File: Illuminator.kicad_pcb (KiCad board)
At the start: 2 copper layers, 60 x 60 mm, 22 parts, among them J0 Conn_01x03_Male, Q0 DMG1012UW

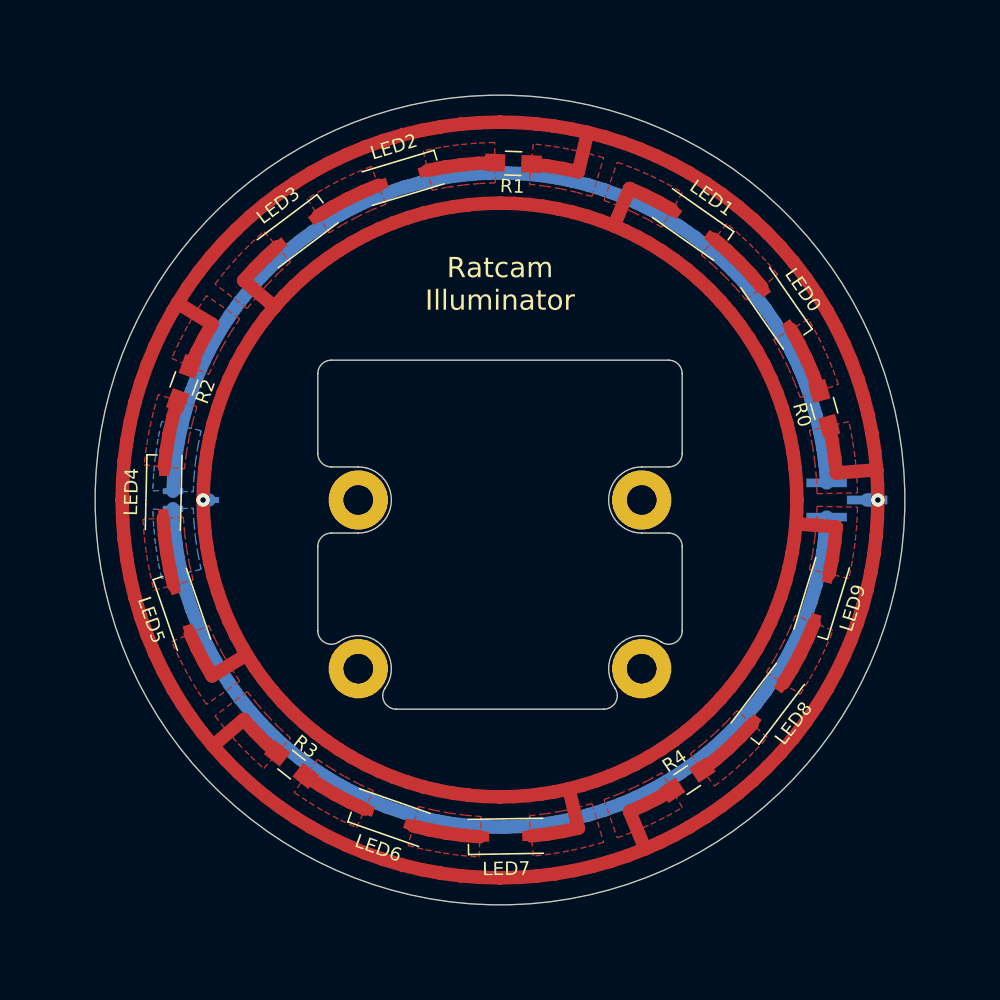
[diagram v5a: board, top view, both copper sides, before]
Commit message: Routing and placing everything from scratch.
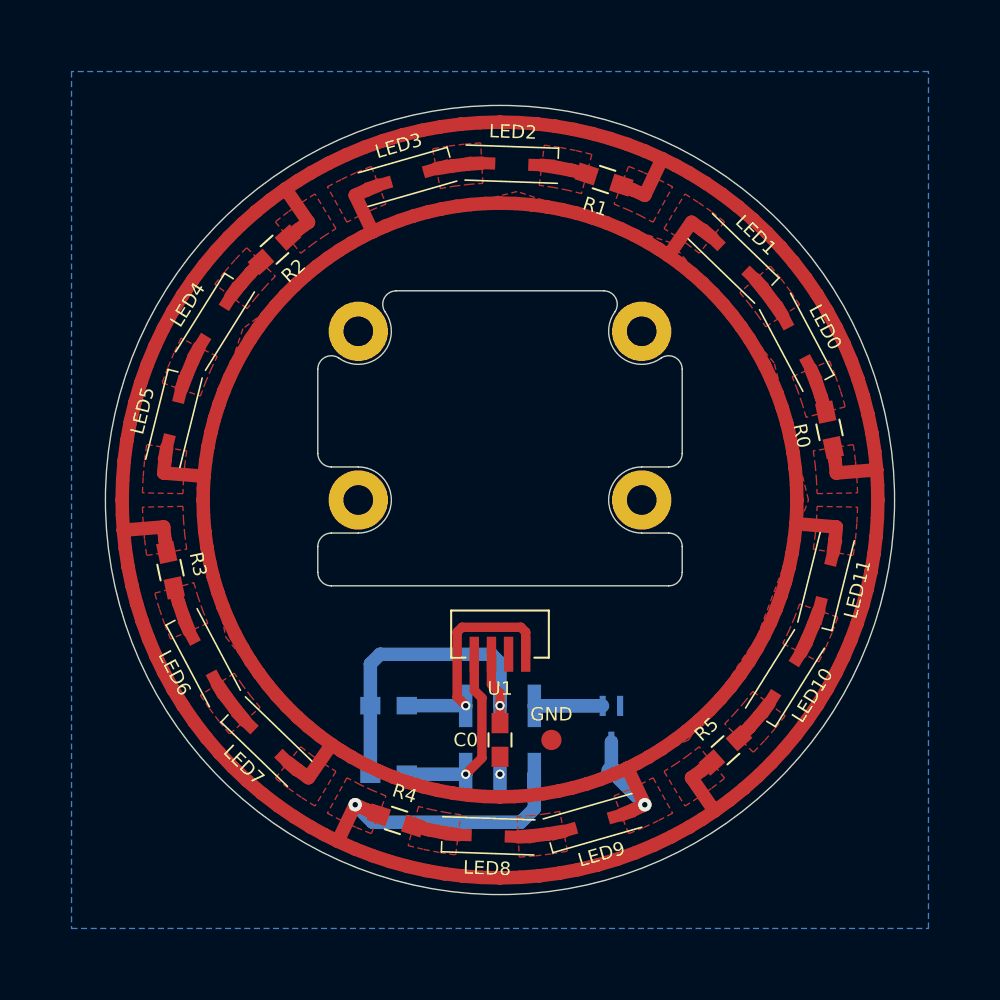
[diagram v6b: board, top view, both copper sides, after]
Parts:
- removed QRCode: http://bit.ly/2m9yLHR, Ratcam:QRCode
- removed the REF** at (110.5, 112.5)
- removed the REF** at (89.5, 112.5)
- added C0: 100nF, Capacitors_SMD:C_0805_HandSoldering, F.Cu at (100.0, 117.8)
- added GND: Measurement_Point_Round-SMD-Pad_Small, Measurement_Points:Measurement_Point_Round-SMD-Pad_Small, F.Cu at (103.8, 117.8)
- added LED: Measurement_Point_Round-SMD-Pad_Small, Measurement_Points:Measurement_Point_Round-SMD-Pad_Small, B.Cu at (108.3, 120.1)
- added LED10: VSMY2850G, Ratcam:LED-GW_2.3x2.3mm_HandSoldering, F.Cu at (121.1, 113.2)
- added LED11: VSMY2850G, Ratcam:LED-GW_2.3x2.3mm_HandSoldering, F.Cu at (124.2, 106.0)
- added R5: 15, Resistors_SMD:R_0805_HandSoldering, F.Cu at (116.7, 118.5)
- added REF**: MountingHole_2.2mm_M2, Mounting_Holes:MountingHole_2.2mm_M2_Pad, F.Cu at (110.5, 87.5)
- added REF**: MountingHole_2.2mm_M2, Mounting_Holes:MountingHole_2.2mm_M2_Pad, F.Cu at (89.5, 87.5)
- added R_PU1: 4.7KΩ, Resistors_SMD:R_0805_HandSoldering, B.Cu at (91.7, 120.3)
- added R_PU2: 4.7KΩ, Resistors_SMD:R_0805_HandSoldering, B.Cu at (91.7, 115.2)
- added U1: VEML7700, Ratcam:VEML7700, F.Cu at (100.0, 111.4)
- J0: value Conn_01x03_Male -> Conn_02x03_Top_Bottom; footprint Pin_Headers:Pin_Header_Straight_1x03_Pitch1.27mm_SMD_Pin1Left -> Pin_Headers:Pin_Header_Straight_2x03_Pitch2.54mm_SMD
- LED0, LED1, LED2, LED3, LED4, LED5, LED6, LED7, LED8, LED9: footprint Ratcam:LED-GW_2.3x2.3mm -> Ratcam:LED-GW_2.3x2.3mm_HandSoldering
- REF** (x2): value MountingHole_2.2mm_M2_Pad -> MountingHole_2.2mm_M2
- moved Q0 35.3 mm to (108.3, 116.6), turned to 270 degrees
- moved J0 31.3 mm to (100.0, 117.8), turned to 90 degrees
- moved LED9 23.8 mm to (106.9, 123.9), turned to 195.975 degrees
- moved LED8 22.9 mm to (99.1, 124.9), turned to 177.989 degrees
- moved R4 21.8 mm to (92.3, 123.7), turned to 342.015 degrees
- moved LED7 19.1 mm to (82.7, 117.9), turned to 135.975 degrees
- moved LED6 18.2 mm to (78.0, 111.7), turned to 117.989 degrees
- moved R3 17.0 mm to (75.6, 105.2), turned to 282.015 degrees
- moved LED5 14.2 mm to (75.8, 94.0), turned to 75.9747 degrees
- moved LED4 13.2 mm to (78.9, 86.8), turned to 57.9894 degrees
- moved R2 12.0 mm to (83.3, 81.5), turned to 222.015 degrees
- moved LED3 9.08 mm to (93.1, 76.1), turned to 15.9747 degrees
- moved LED2 8.12 mm to (100.9, 75.1), turned to 357.989 degrees
- moved R1 6.84 mm to (107.7, 76.3), turned to 162.015 degrees
- moved LED1 3.91 mm to (117.3, 82.1), turned to 315.975 degrees
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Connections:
- J0 pad 1: /TO_3V3 -> /TO_5V
- J0 pad 2: /TO_5V -> /TO_PWM
- Q0 pad 1: /TO_3V3 -> /TO_PWM
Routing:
- net /TO_GND: track 74.2 -> 0.00 mm, vias 0 -> 1
- net /TO_3V3: track 74.2 -> 27.5 mm, vias 0 -> 1
- net /TO_SDA: track 0.00 -> 17.1 mm, vias 0 -> 1
- net /TO_5V: track 209.3 -> 223.9 mm
- net /TO_SCL: track 0.00 -> 14.0 mm, vias 0 -> 1
- net /TO_PWM: track 0.00 -> 5.09 mm
- net Net-(LED10-Pad2): track 0.00 -> 3.39 mm
- net Net-(LED10-Pad1): track 0.00 -> 3.39 mm
- net Net-(LED1-Pad1): track 171.3 -> 173.3 mm
- net Net-(LED4-Pad1): track 5.03 -> 3.39 mm
- net Net-(LED8-Pad1): track 5.03 -> 3.39 mm
- net Net-(LED8-Pad2): track 5.03 -> 3.39 mm
- net Net-(LED6-Pad1): track 5.03 -> 3.39 mm
- net Net-(LED0-Pad2): track 5.03 -> 3.39 mm
- net Net-(LED2-Pad2): track 5.03 -> 3.39 mm
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- added copper zone on F.Cu, net /TO_GND
- added copper zone on F.Cu, net Net-(LED10-Pad1)
- added copper zone on F.Cu, net Net-(LED10-Pad2)
- removed copper zone on B.Cu, net /TO_3V3
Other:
- board size 60 x 60 mm -> 58.5 x 58.5 mm
- net class Sensor added: clearance 0.2, trace_width 0.7, via_dia 0.7, via_drill 0.4
- rule trace_min: 1 -> 0.2
- rule via_min_drill: 0.4 -> 0.3
- rule via_min_size: 1 -> 0.4
- board text added: "+5V GND SCL"
- board text added: "PWM 3V3 SDA"
- board text removed: "3V3"
- board text removed: "5V"
- board text removed: "GND"
- board text removed: "Ratcam Illuminator"

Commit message: Added models to R and C for rendering.
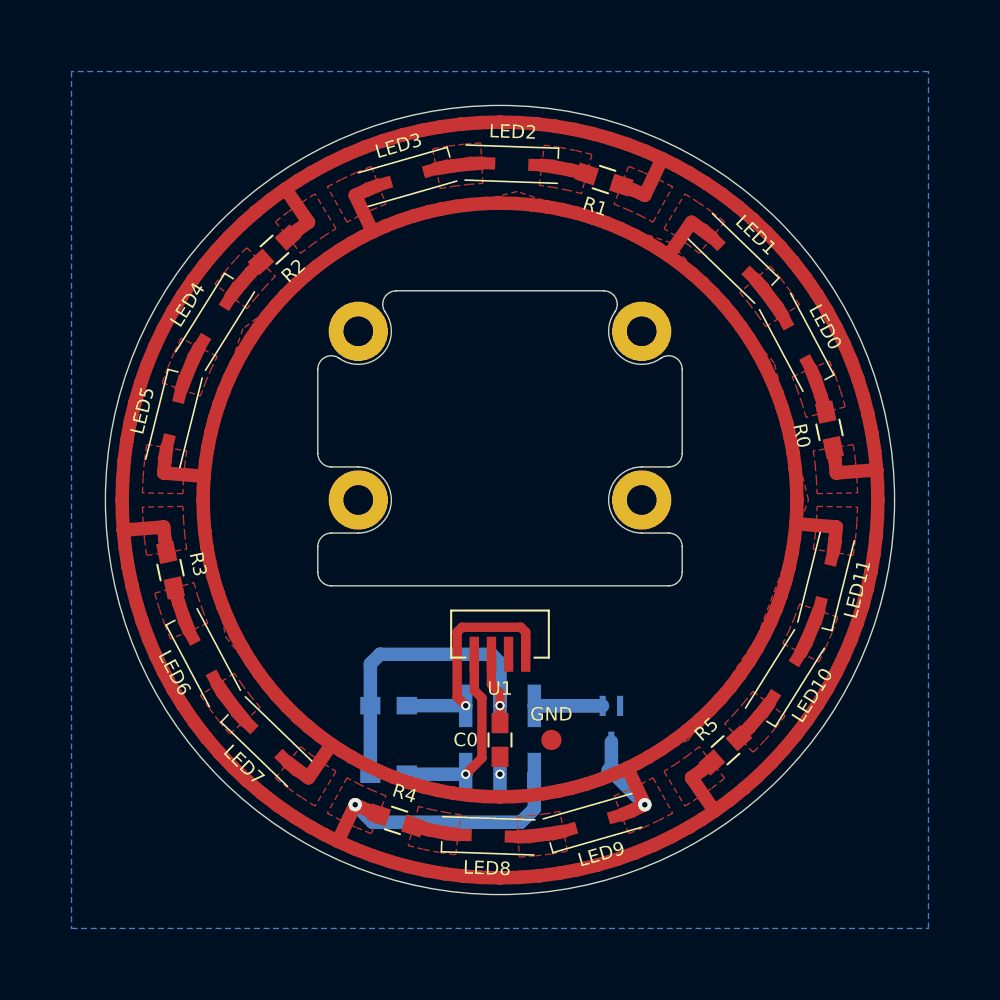
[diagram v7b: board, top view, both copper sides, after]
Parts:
- turned R0 to 102 degrees
- turned R1 to 162 degrees
- turned R2 to 222 degrees
- turned R3 to 282 degrees
- turned R4 to 342 degrees
- turned R5 to 42 degrees
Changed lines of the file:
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@@
   (page A4)
   (layers
-    (0 F.Cu signal)
+    (0 F.Cu signal hide)
     (31 B.Cu signal)
     (32 B.Adhes user)
@@
     (aux_axis_origin 0 0)
     (grid_origin 100 100)
-    (visible_elements FFFFFF7F)
+    (visible_elements FFFF7F7F)
     (pcbplotparams
       (layerselection 0x010fc_ffffffff)
@@
       (rotate (xyz 0 0 0))
     )
+    (model ${KISYS3DMOD}/Resistors_SMD.3dshapes/R_0805.wrl
+      (at (xyz 0 0 0))
+      (scale (xyz 1 1 1))
+      (rotate (xyz 0 0 0))
+    )
   )
   (module Mounting_Holes:MountingHole_2.2mm_M2_Pad (layer F.Cu)
@@
       (net 2 /TO_3V3))
     (model Capacitors_SMD.3dshapes/C_0805_HandSoldering.wrl
+      (at (xyz 0 0 0))
+      (scale (xyz 1 1 1))
+      (rotate (xyz 0 0 0))
+    )
+    (model ${KISYS3DMOD}/Capacitors_SMD.3dshapes/C_0805.wrl
       (at (xyz 0 0 0))
       (scale (xyz 1 1 1))
@@
   )
   (module Resistors_SMD:R_0805_HandSoldering (layer F.Cu)
-    (at 124.416682 94.803546 102.0146544)
+    (at 124.416682 94.803546 102)
     (descr "Resistor SMD 0805, hand soldering")
     (tags "resistor 0805")
     (attr smd)
-    (fp_text reference R0 (at 0 -2.1 102.0146544) (layer F.SilkS)
-      (effects (font (size 1 1) (thickness 0.15)))
-    )
-    (fp_text value 15 (at 0 2.1 102.0146544) (layer F.Fab)
+    (fp_text reference R0 (at 0 -2.1 102) (layer F.SilkS)
+      (effects (font (size 1 1) (thickness 0.15)))
+    )
+    (fp_text value 15 (at 0 2.1 102) (layer F.Fab)
       (effects (font (size 1 1) (thickness 0.15)))
     )
@@
     (fp_line (start 0.6 0.875) (end -0.6 0.875) (layer F.SilkS) (width 0.15))
     (fp_line (start -0.6 -0.875) (end 0.6 -0.875) (layer F.SilkS) (width 0.15))
-    (pad 1 smd rect (at -1.35 0.000001 102.0146544) (size 1.5 1.3) (layers F.Cu F.Paste F.Mask)
+    (pad 1 smd rect (at -1.35 0.000001 102) (size 1.5 1.3) (layers F.Cu F.Paste F.Mask)
       (net 3 /TO_5V))
-    (pad 2 smd rect (at 1.35 -0.000001 102.0146544) (size 1.5 1.3) (layers F.Cu F.Paste F.Mask)
+    (pad 2 smd rect (at 1.35 -0.000001 102) (size 1.5 1.3) (layers F.Cu F.Paste F.Mask)
       (net 8 "Net-(LED0-Pad2)"))
     (model Resistors_SMD.3dshapes/R_0805_HandSoldering.wrl
@@
       (rotate (xyz 0 0 0))
     )
+    (model ${KISYS3DMOD}/Resistors_SMD.3dshapes/R_0805.wrl
+      (at (xyz 0 0 0))
+      (scale (xyz 1 1 1))
+      (rotate (xyz 0 0 0))
+    )
   )
   (module Resistors_SMD:R_0805_HandSoldering (layer F.Cu)
-    (at 107.70808 76.256306 162.0146544)
+    (at 107.70808 76.256306 162)
     (descr "Resistor SMD 0805, hand soldering")
     (tags "resistor 0805")
     (attr smd)
-    (fp_text reference R1 (at 0 -2.1 162.0146544) (layer F.SilkS)
-      (effects (font (size 1 1) (thickness 0.15)))
-    )
-    (fp_text value 15 (at 0 2.1 162.0146544) (layer F.Fab)
+    (fp_text reference R1 (at 0 -2.1 162) (layer F.SilkS)
+      (effects (font (size 1 1) (thickness 0.15)))
+    )
+    (fp_text value 15 (at 0 2.1 162) (layer F.Fab)
       (effects (font (size 1 1) (thickness 0.15)))
     )
@@
     (fp_line (start 1 0.625) (end -1 0.625) (layer F.Fab) (width 0.1))
     (fp_line (start -1 0.625) (end -1 -0.625) (layer F.Fab) (width 0.1))
-    (pad 2 smd rect (at 1.35 0 162.0146544) (size 1.5 1.3) (layers F.Cu F.Paste F.Mask)
+    (pad 2 smd rect (at 1.35 0 162) (size 1.5 1.3) (layers F.Cu F.Paste F.Mask)
       (net 11 "Net-(LED2-Pad2)"))
-    (pad 1 smd rect (at -1.35 0 162.0146544) (size 1.5 1.3) (layers F.Cu F.Paste F.Mask)
+    (pad 1 smd rect (at -1.35 0 162) (size 1.5 1.3) (layers F.Cu F.Paste F.Mask)
       (net 3 /TO_5V))
     (model Resistors_SMD.3dshapes/R_0805_HandSoldering.wrl
@@
       (rotate (xyz 0 0 0))
     )
+    (model ${KISYS3DMOD}/Resistors_SMD.3dshapes/R_0805.wrl
+      (at (xyz 0 0 0))
+      (scale (xyz 1 1 1))
+      (rotate (xyz 0 0 0))
+    )
   )
   (module Resistors_SMD:R_0805_HandSoldering (layer F.Cu)
-    (at 83.291398 81.452759 222.0146544)
+    (at 83.291398 81.452759 222)
     (descr "Resistor SMD 0805, hand soldering")
     (tags "resistor 0805")
     (attr smd)
-    (fp_text reference R2 (at 0 -2.1 222.0146544) (layer F.SilkS)
-      (effects (font (size 1 1) (thickness 0.15)))
-    )
-    (fp_text value 15 (at 0 2.1 222.0146544) (layer F.Fab)
+    (fp_text reference R2 (at 0 -2.1 222) (layer F.SilkS)
+      (effects (font (size 1 1) (thickness 0.15)))
+    )
+    (fp_text value 15 (at 0 2.1 222) (layer F.Fab)
       (effects (font (size 1 1) (thickness 0.15)))
     )
@@
     (fp_line (start 0.6 0.875) (end -0.6 0.875) (layer F.SilkS) (width 0.15))
     (fp_line (start -0.6 -0.875) (end 0.6 -0.875) (layer F.SilkS) (width 0.15))
-    (pad 1 smd rect (at -1.35 0 222.0146544) (size 1.5 1.3) (layers F.Cu F.Paste F.Mask)
+    (pad 1 smd rect (at -1.35 0 222) (size 1.5 1.3) (layers F.Cu F.Paste F.Mask)
       (net 3 /TO_5V))
-    (pad 2 smd rect (at 1.35 0 222.0146544) (size 1.5 1.3) (layers F.Cu F.Paste F.Mask)
+    (pad 2 smd rect (at 1.35 0 222) (size 1.5 1.3) (layers F.Cu F.Paste F.Mask)
       (net 13 "Net-(LED4-Pad2)"))
     (model Resistors_SMD.3dshapes/R_0805_HandSoldering.wrl
@@
       (rotate (xyz 0 0 0))
     )
+    (model ${KISYS3DMOD}/Resistors_SMD.3dshapes/R_0805.wrl
+      (at (xyz 0 0 0))
+      (scale (xyz 1 1 1))
+      (rotate (xyz 0 0 0))
+    )
   )
   (module Resistors_SMD:R_0805_HandSoldering (layer F.Cu)
-    (at 75.583317 105.196453 282.0146544)
+    (at 75.583317 105.196453 282)
     (descr "Resistor SMD 0805, hand soldering")
     (tags "resistor 0805")
     (attr smd)
-    (fp_text reference R3 (at 0 -2.1 282.0146544) (layer F.SilkS)
-      (effects (font (size 1 1) (thickness 0.15)))
-    )
-    (fp_text value 15 (at 0 2.1 282.0146544) (layer F.Fab)
+    (fp_text reference R3 (at 0 -2.1 282) (layer F.SilkS)
+      (effects (font (size 1 1) (thickness 0.15)))
+    )
+    (fp_text value 15 (at 0 2.1 282) (layer F.Fab)
       (effects (font (size 1 1) (thickness 0.15)))
     )
@@
     (fp_line (start 1 0.625) (end -1 0.625) (layer F.Fab) (width 0.1))
     (fp_line (start -1 0.625) (end -1 -0.625) (layer F.Fab) (width 0.1))
-    (pad 2 smd rect (at 1.35 -0.000001 282.0146544) (size 1.5 1.3) (layers F.Cu F.Paste F.Mask)
+    (pad 2 smd rect (at 1.35 -0.000001 282) (size 1.5 1.3) (layers F.Cu F.Paste F.Mask)
       (net 15 "Net-(LED6-Pad2)"))
-    (pad 1 smd rect (at -1.35 0.000001 282.0146544) (size 1.5 1.3) (layers F.Cu F.Paste F.Mask)
+    (pad 1 smd rect (at -1.35 0.000001 282) (size 1.5 1.3) (layers F.Cu F.Paste F.Mask)
       (net 3 /TO_5V))
     (model Resistors_SMD.3dshapes/R_0805_HandSoldering.wrl
@@
       (rotate (xyz 0 0 0))
     )
+    (model ${KISYS3DMOD}/Resistors_SMD.3dshapes/R_0805.wrl
+      (at (xyz 0 0 0))
+      (scale (xyz 1 1 1))
+      (rotate (xyz 0 0 0))
+    )
   )
   (module Resistors_SMD:R_0805_HandSoldering (layer F.Cu)
-    (at 92.291919 123.743693 342.0146544)
+    (at 92.291919 123.743693 342)
     (descr "Resistor SMD 0805, hand soldering")
     (tags "resistor 0805")
     (attr smd)
-    (fp_text reference R4 (at 0 -2.1 342.0146544) (layer F.SilkS)
-      (effects (font (size 1 1) (thickness 0.15)))
-    )
-    (fp_text value 15 (at 0 2.1 342.0146544) (layer F.Fab)
+    (fp_text reference R4 (at 0 -2.1 342) (layer F.SilkS)
+      (effects (font (size 1 1) (thickness 0.15)))
+    )
+    (fp_text value 15 (at 0 2.1 342) (layer F.Fab)
       (effects (font (size 1 1) (thickness 0.15)))
     )
@@
     (fp_line (start 0.6 0.875) (end -0.6 0.875) (layer F.SilkS) (width 0.15))
     (fp_line (start -0.6 -0.875) (end 0.6 -0.875) (layer F.SilkS) (width 0.15))
-    (pad 1 smd rect (at -1.35 0 342.0146544) (size 1.5 1.3) (layers F.Cu F.Paste F.Mask)
+    (pad 1 smd rect (at -1.35 0 342) (size 1.5 1.3) (layers F.Cu F.Paste F.Mask)
       (net 3 /TO_5V))
-    (pad 2 smd rect (at 1.35 0 342.0146544) (size 1.5 1.3) (layers F.Cu F.Paste F.Mask)
+    (pad 2 smd rect (at 1.35 0 342) (size 1.5 1.3) (layers F.Cu F.Paste F.Mask)
       (net 17 "Net-(LED8-Pad2)"))
     (model Resistors_SMD.3dshapes/R_0805_HandSoldering.wrl
@@
       (rotate (xyz 0 0 0))
     )
+    (model ${KISYS3DMOD}/Resistors_SMD.3dshapes/R_0805.wrl
+      (at (xyz 0 0 0))
+      (scale (xyz 1 1 1))
+      (rotate (xyz 0 0 0))
+    )
   )
   (module Resistors_SMD:R_0805_HandSoldering (layer F.Cu)
-    (at 116.708601 118.54724 42.01465443)
+    (at 116.708601 118.54724 42)
     (descr "Resistor SMD 0805, hand soldering")
     (tags "resistor 0805")
     (attr smd)
-    (fp_text reference R5 (at 0 -2.1 42.01465443) (layer F.SilkS)
-      (effects (font (size 1 1) (thickness 0.15)))
-    )
-    (fp_text value 15 (at 0 2.1 42.01465443) (layer F.Fab)
+    (fp_text reference R5 (at 0 -2.1 42) (layer F.SilkS)
+      (effects (font (size 1 1) (thickness 0.15)))
+    )
+    (fp_text value 15 (at 0 2.1 42) (layer F.Fab)
       (effects (font (size 1 1) (thickness 0.15)))
     )
@@
     (fp_line (start 1 0.625) (end -1 0.625) (layer F.Fab) (width 0.1))
     (fp_line (start -1 0.625) (end -1 -0.625) (layer F.Fab) (width 0.1))
-    (pad 2 smd rect (at 1.35 0 42.01465443) (size 1.5 1.3) (layers F.Cu F.Paste F.Mask)
+    (pad 2 smd rect (at 1.35 0 42) (size 1.5 1.3) (layers F.Cu F.Paste F.Mask)
       (net 18 "Net-(LED10-Pad2)"))
-    (pad 1 smd rect (at -1.35 0 42.01465443) (size 1.5 1.3) (layers F.Cu F.Paste F.Mask)
+    (pad 1 smd rect (at -1.35 0 42) (size 1.5 1.3) (layers F.Cu F.Paste F.Mask)
       (net 3 /TO_5V))
     (model Resistors_SMD.3dshapes/R_0805_HandSoldering.wrl
+      (at (xyz 0 0 0))
+      (scale (xyz 1 1 1))
+      (rotate (xyz 0 0 0))
+    )
+    (model ${KISYS3DMOD}/Resistors_SMD.3dshapes/R_0805.wrl
       (at (xyz 0 0 0))
       (scale (xyz 1 1 1))
@@
       (at (xyz 0 0 0))
       (scale (xyz 1 1 1))
+      (rotate (xyz 0 0 0))
+    )
+    (model ${KISYS3DMOD}/Resistors_SMD.3dshapes/R_0805.wrl
+      (at (xyz 0 0 0))
+      (scale (xyz 1 1 1))
